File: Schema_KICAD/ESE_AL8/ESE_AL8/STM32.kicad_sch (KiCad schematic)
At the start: 24 parts, among them J2 Conn_ST_STDC14, U1 STM32G431CBUx, Y1 16MHz

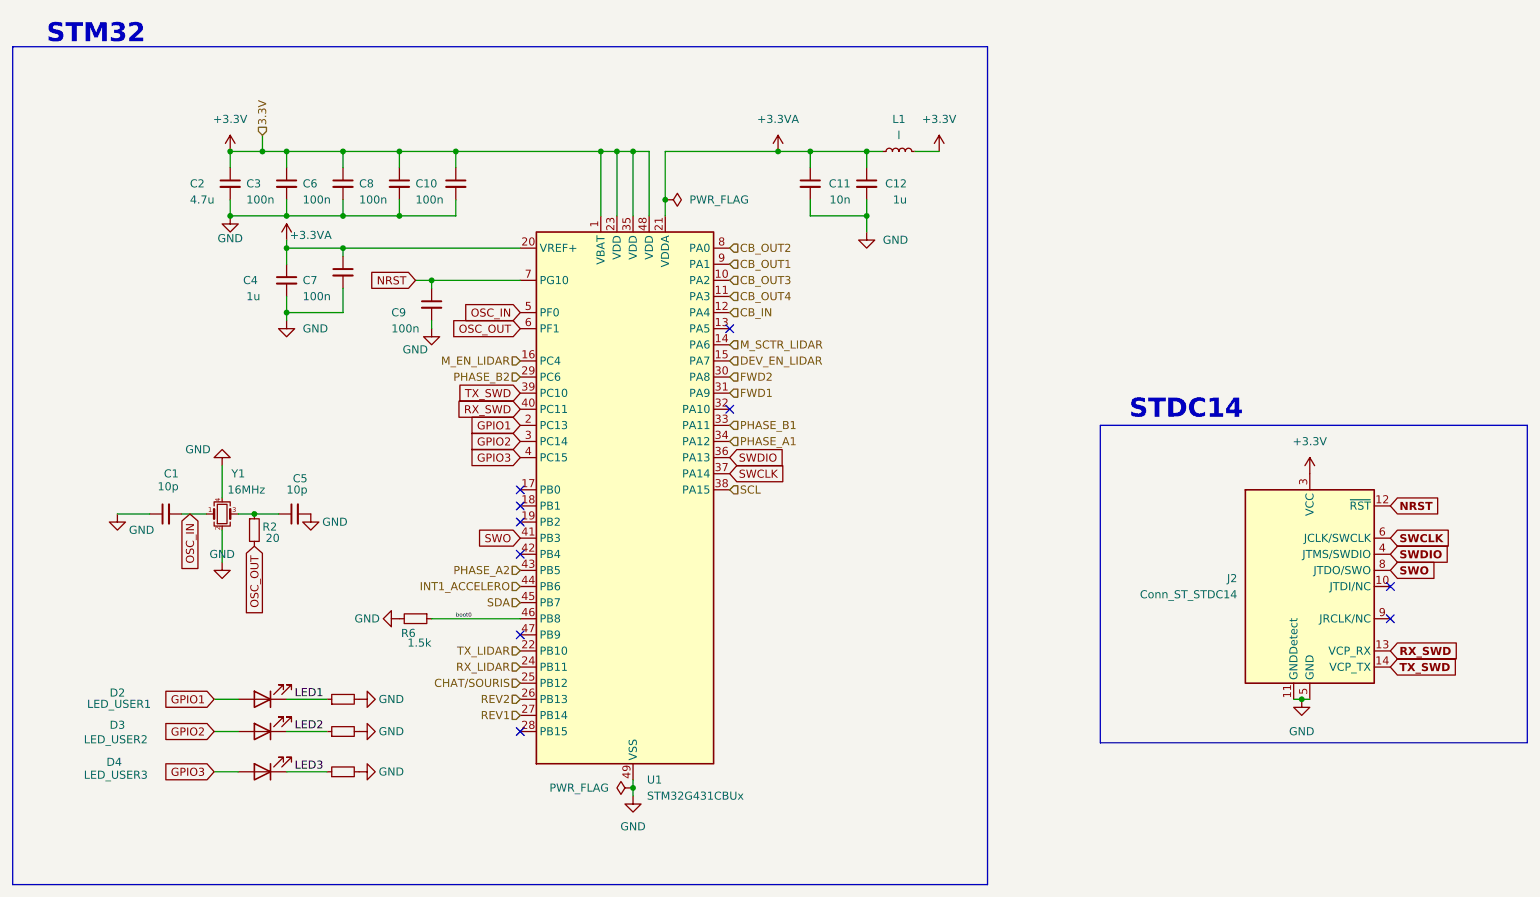
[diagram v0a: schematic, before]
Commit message: Routage aprés correction
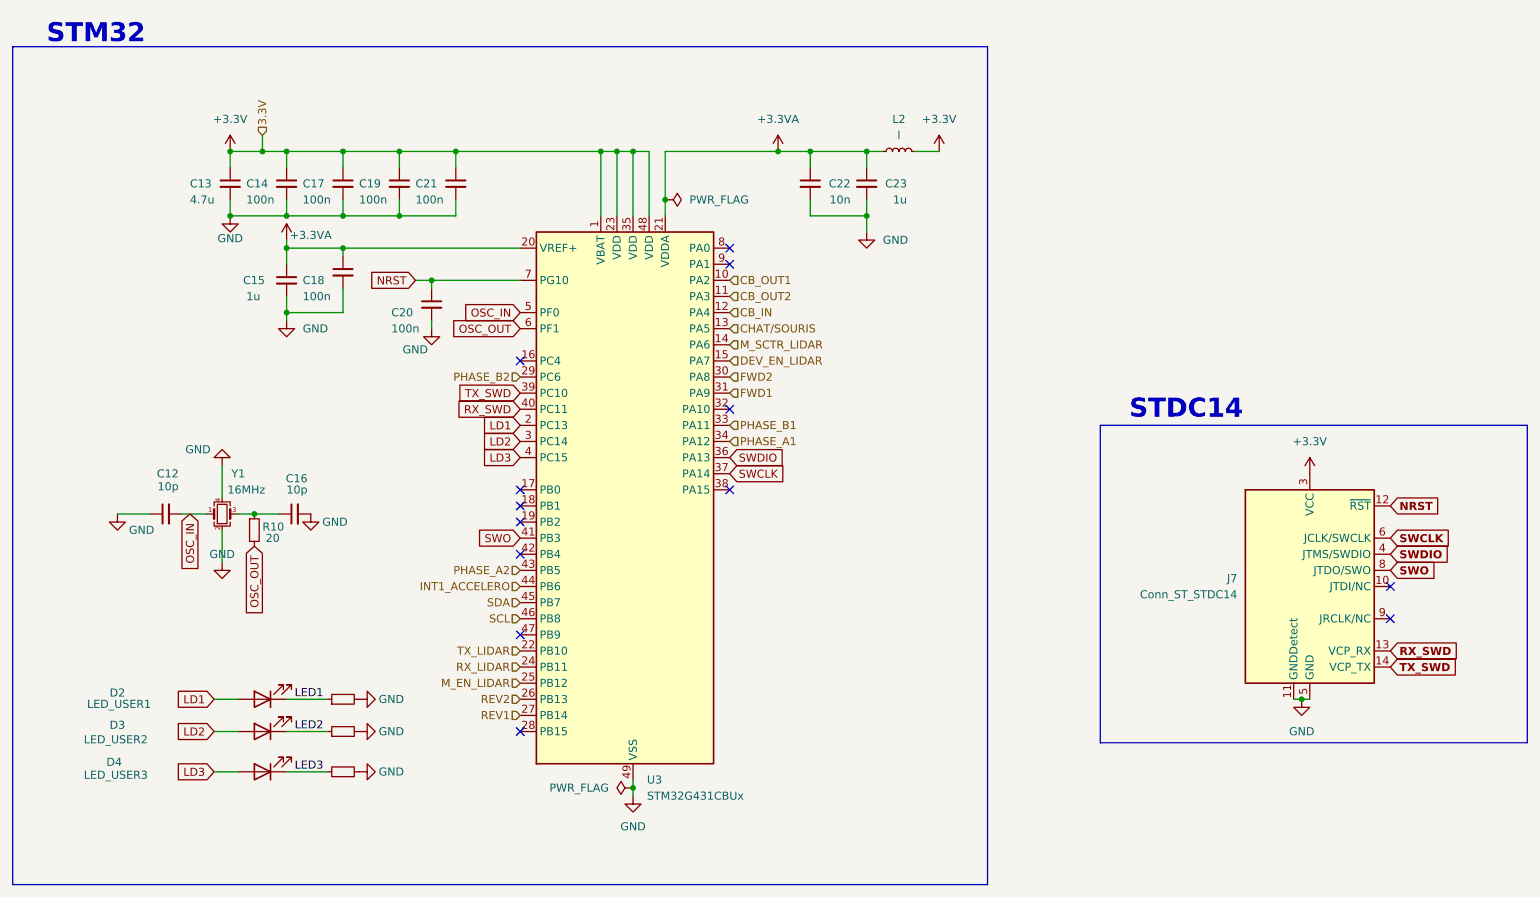
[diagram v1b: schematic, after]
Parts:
- removed R6: 1.5k, Resistor_SMD:R_0402_1005Metric_Pad0.72x0.64mm_HandSolder, symbol Device:R_Small
- C12: renamed from C1; footprint Capacitor_SMD:C_0402_1005Metric_Pad0.74x0.62mm_HandSolder -> Capacitor_SMD:C_0402_1005Metric
- C13: renamed from C2; footprint Capacitor_SMD:C_0603_1608Metric_Pad1.08x0.95mm_HandSolder -> Capacitor_SMD:C_0603_1608Metric
- C14: renamed from C3; footprint Capacitor_SMD:C_0402_1005Metric_Pad0.74x0.62mm_HandSolder -> Capacitor_SMD:C_0402_1005Metric
- C15: renamed from C4; footprint Capacitor_SMD:C_0402_1005Metric_Pad0.74x0.62mm_HandSolder -> Capacitor_SMD:C_0603_1608Metric
- C16: renamed from C5; footprint Capacitor_SMD:C_0402_1005Metric_Pad0.74x0.62mm_HandSolder -> Capacitor_SMD:C_0402_1005Metric
- C17: renamed from C6; footprint Capacitor_SMD:C_0402_1005Metric_Pad0.74x0.62mm_HandSolder -> Capacitor_SMD:C_0402_1005Metric
- C18: renamed from C7; footprint Capacitor_SMD:C_0402_1005Metric_Pad0.74x0.62mm_HandSolder -> Capacitor_SMD:C_0402_1005Metric
- C19: renamed from C8; footprint Capacitor_SMD:C_0402_1005Metric_Pad0.74x0.62mm_HandSolder -> Capacitor_SMD:C_0402_1005Metric
- C20: renamed from C9; footprint Capacitor_SMD:C_0402_1005Metric_Pad0.74x0.62mm_HandSolder -> Capacitor_SMD:C_0402_1005Metric
- C21: renamed from C10; footprint Capacitor_SMD:C_0402_1005Metric_Pad0.74x0.62mm_HandSolder -> Capacitor_SMD:C_0402_1005Metric
- C22: renamed from C11; footprint Capacitor_SMD:C_0402_1005Metric_Pad0.74x0.62mm_HandSolder -> Capacitor_SMD:C_0402_1005Metric
- C23: renamed from C12; footprint Capacitor_SMD:C_0402_1005Metric_Pad0.74x0.62mm_HandSolder -> Capacitor_SMD:C_0603_1608Metric
- D2, D3, D4: footprint Resistor_SMD:R_0402_1005Metric_Pad0.72x0.64mm_HandSolder -> LED_SMD:LED_0603_1608Metric
- R10: renamed from R2; footprint Resistor_SMD:R_0402_1005Metric_Pad0.72x0.64mm_HandSolder -> Resistor_SMD:R_0402_1005Metric
- R11: renamed from R3; footprint Resistor_SMD:R_0402_1005Metric_Pad0.72x0.64mm_HandSolder -> Resistor_SMD:R_0402_1005Metric
- R12: renamed from R4; footprint Resistor_SMD:R_0402_1005Metric_Pad0.72x0.64mm_HandSolder -> Resistor_SMD:R_0402_1005Metric
- R13: renamed from R5; footprint Resistor_SMD:R_0402_1005Metric_Pad0.72x0.64mm_HandSolder -> Resistor_SMD:R_0402_1005Metric
- renumbered J2 to J7, L1 to L2, U1 to U3
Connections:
- net CB_OUT3 is gone; now on net CB_OUT1: U3.10 (PA2)
- net CB_OUT4 is gone; now on net CB_OUT2: U3.11 (PA3)
- net boot0 is gone; now on net SCL: U3.46 (PB8)
- net CB_OUT1: no longer U3.9 (PA1)
- net CB_OUT2: no longer U3.8 (PA0)
- net CHAT/SOURIS: now also U3.13 (PA5); no longer U3.25 (PB12)
- net M_EN_LIDAR: now also U3.25 (PB12); no longer U3.16 (PC4)
- net SCL: no longer U3.38 (PA15)
- net GPIO1 renamed LD1
- net GPIO2 renamed LD2
- net GPIO3 renamed LD3
- no-connect marks 10 -> 13

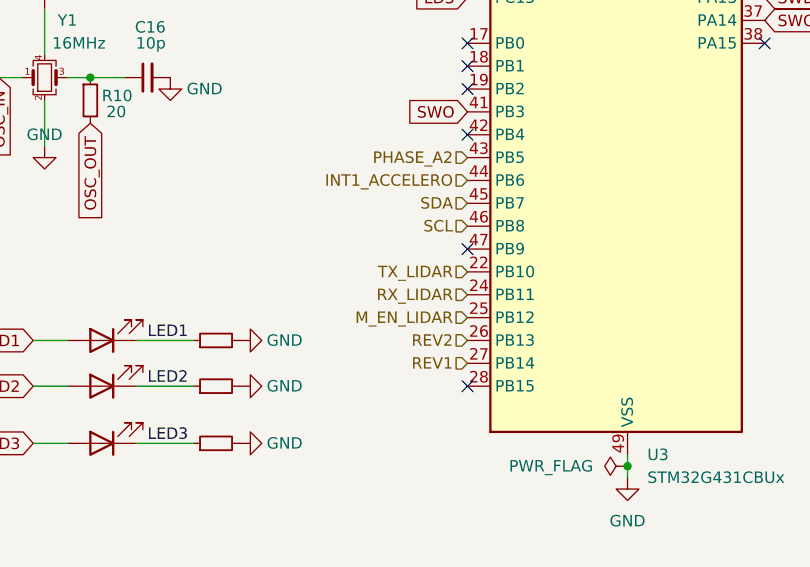
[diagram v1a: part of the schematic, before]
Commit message: Routage aprés correction
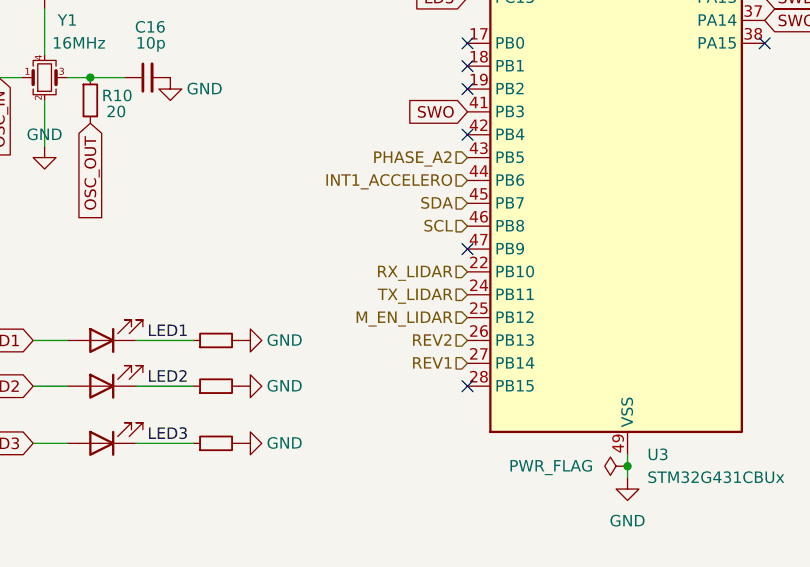
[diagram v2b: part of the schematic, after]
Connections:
- net RX_LIDAR: now also U3.22 (PB10); no longer U3.24 (PB11)
- net TX_LIDAR: now also U3.24 (PB11); no longer U3.22 (PB10)
